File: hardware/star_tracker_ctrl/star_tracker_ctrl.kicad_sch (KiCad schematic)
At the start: 65 parts, among them J1 12V IN, J10 I2C EXP, J11 SPARE IO, J2 CAM USB-A, J20 ESP32 L, J21 ESP32 R, J3 CAM 5V, J30 TMC2209 L, J31 TMC2209 R, J4 MOTOR, J5 DIAG, J6 DS3231, J7 AS5600, J8 HOME, J9 GPS v2, Q1 IRF4905, Q2 IRF4905, Q3 2N3904, SW1 CONFIG, U2 LM2596T-5.0

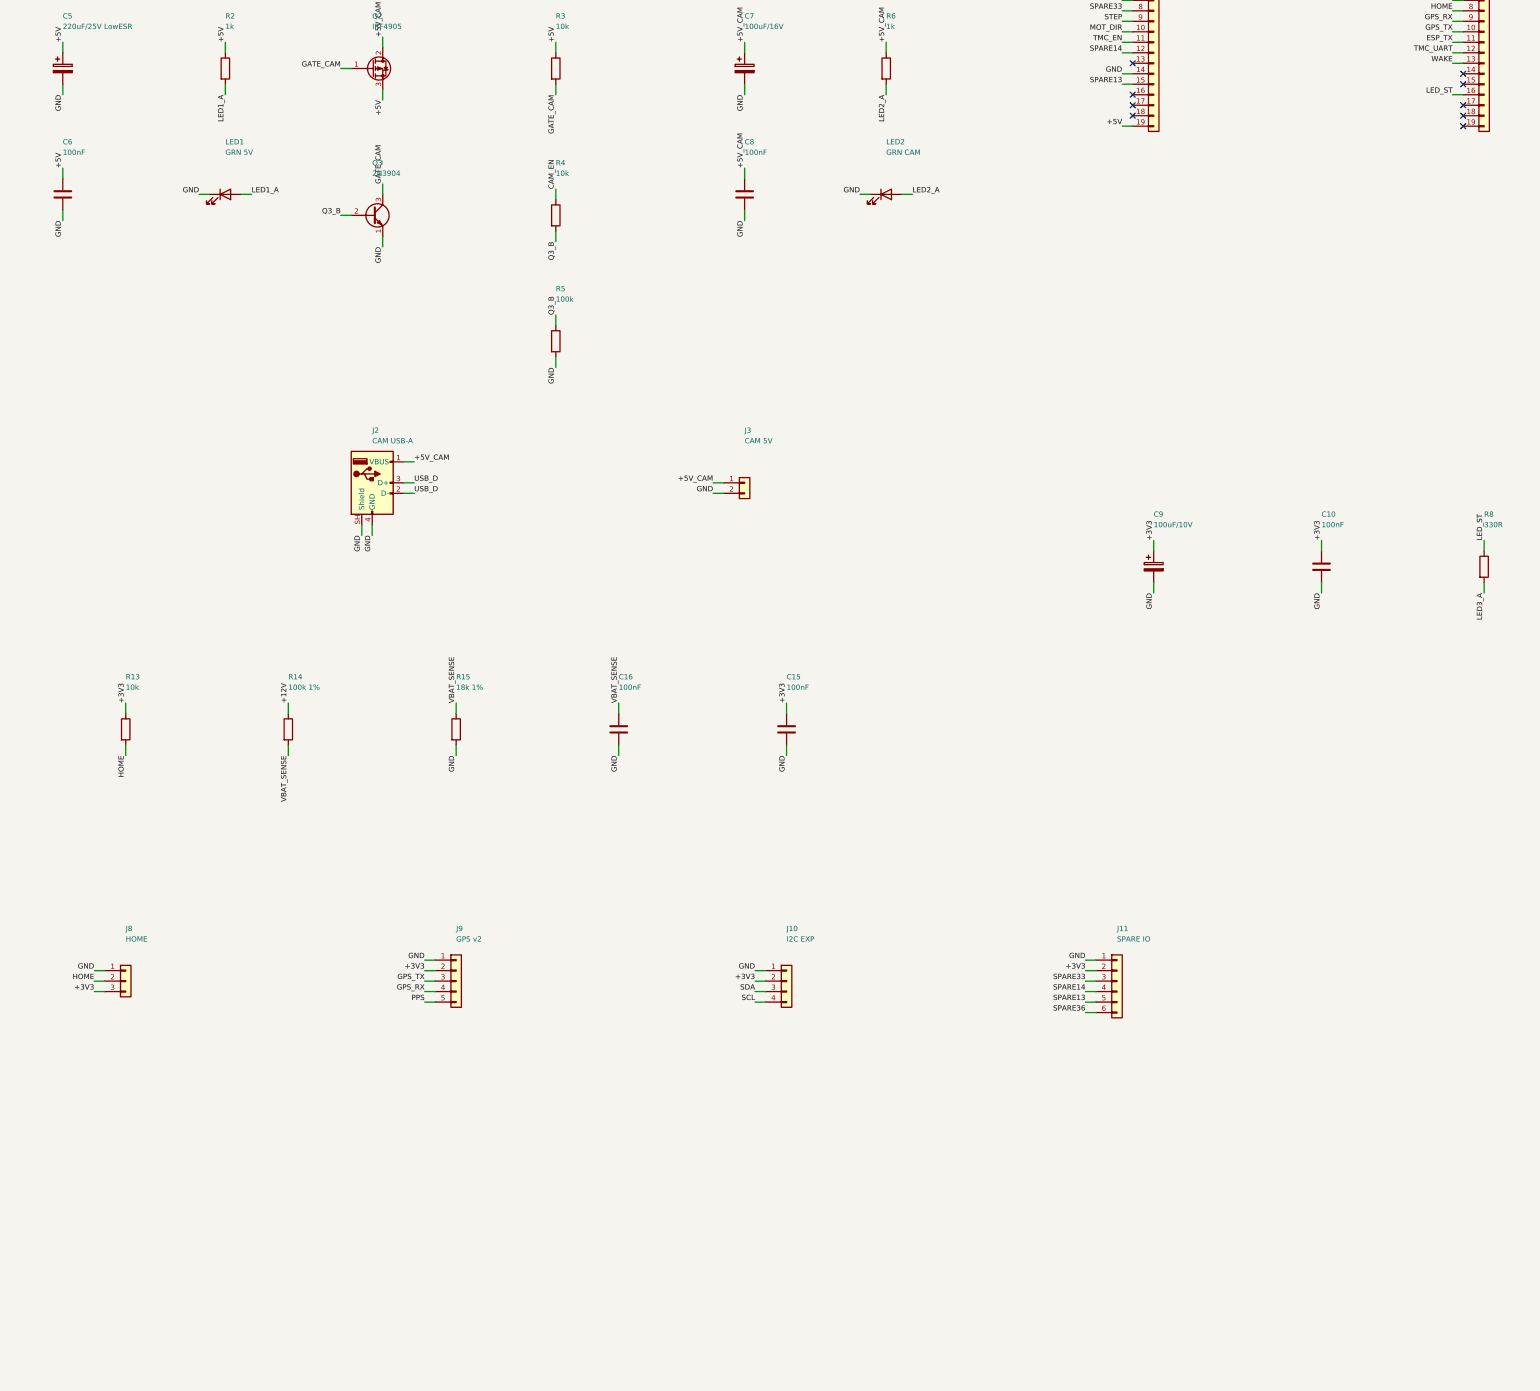
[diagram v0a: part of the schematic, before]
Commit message: Rev B: fix a mirrored ESP32 socket, add GPS, grow the board to 150x100
The important one first. The ESP32 socket in rev A was MIRRORED. The module's
left column was on the top row with pin 1 at the left, and that combination is
neither of the two legal placements -- the transform from module coordinates
to board coordinates had determinant -1, so the module would have had to be
flipped over to fit. Every pin was on the wrong signal. Fabricated, it would
have been scrap with no obvious cause.

A DevKitC laid on its side has exactly two legal orientations:

  90 CW : left column = TOP row, pin 1 at the RIGHT, USB at the LEFT
  90 CCW: left column = BOTTOM row, pin 1 at the LEFT, USB at the RIGHT

Both sockets are now at rotation 270, pin 1 at the right-hand end, USB
pointing left. The rule is written into place.py so it cannot be lost again.

Silkscreen now makes it checkable by eye, which is the real defence: dashed
body outlines for the ESP32 and the TMC2209, a large "USB <<<" at the correct
end, a bold "1" beside pin 1 of all four sockets, per-pin signal names on
every connector, and the orientation stated in words under the module.

GPS is in, as v1 rather than a v2 reservation. A GY-NEO6MV2 supplies time,
date and position; the DS3231 stays, because a GPS cannot wake a sleeping
ESP32 at a time, needs sky view and ~45 mA just to know the time, and has
nothing to say under cloud. The RTC is the bootstrap and the GPS disciplines
it: TIME_SYNC sets the RTC from GPS UTC each evening, records the drift as a
free nightly measurement of the crystal, takes lat/lon for the twilight
calculation, then powers the GPS down. gps_policy defaults to best_effort --
no fix must never cost a night.

The GPS gets a 2N3906 high-side switch off 5 V driven by a 2N3904 on GPIO 2.
Both rails stay up through deep sleep, so an unswitched module would draw
30-45 mA around the clock, roughly 5 Wh a day for a part with ninety seconds
of work each evening. Switched, it costs under 0.1 Wh a nigh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
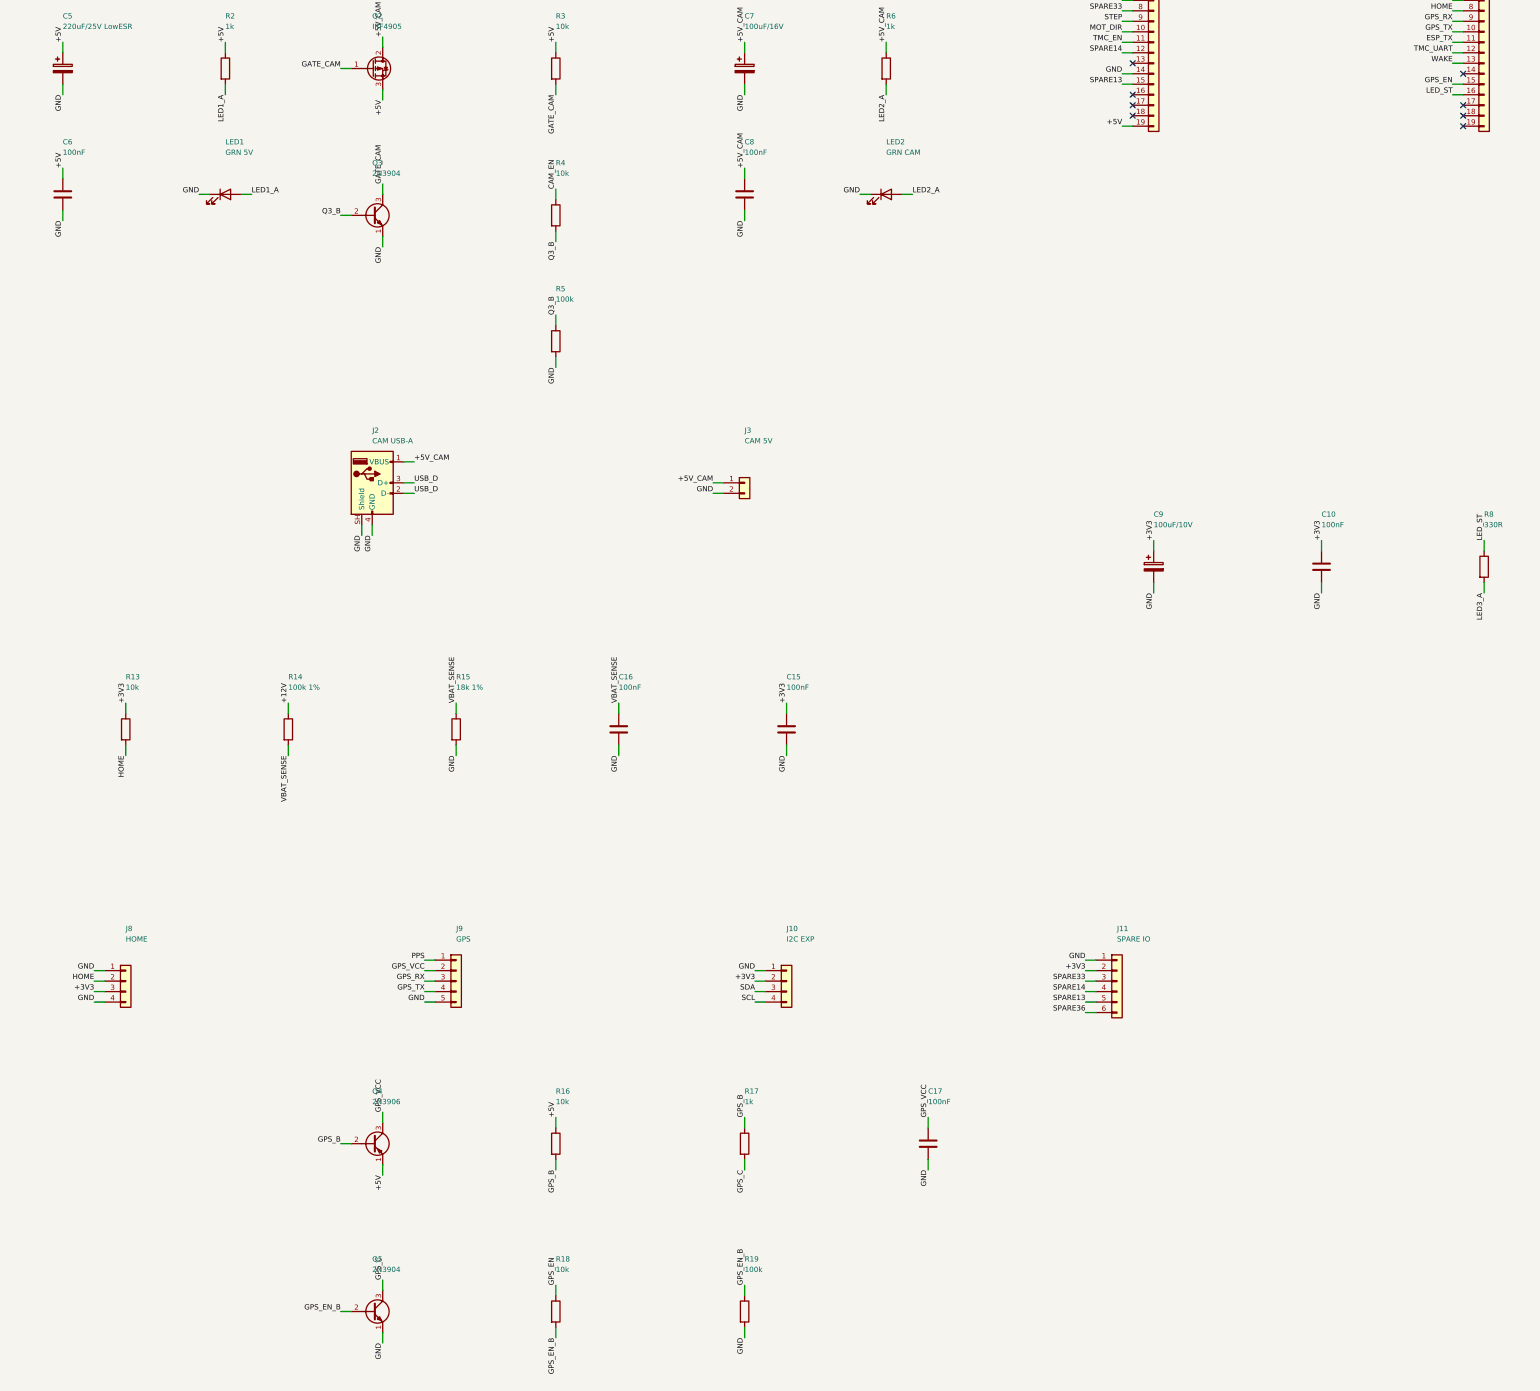
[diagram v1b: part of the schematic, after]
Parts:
- removed J8: HOME, Connector_PinHeader_2.54mm:PinHeader_1x03_P2.54mm_Vertical, symbol Connector_Generic:Conn_01x03
- added C17: 100nF, Capacitor_THT:C_Disc_D5.0mm_W2.5mm_P2.50mm, symbol Device:C
- added J8: HOME, Connector_PinHeader_2.54mm:PinHeader_1x04_P2.54mm_Vertical, symbol Connector_Generic:Conn_01x04
- added Q4: 2N3906, Package_TO_SOT_THT:TO-92_Inline_Wide, symbol Transistor_BJT:2N3906
- added Q5: 2N3904, Package_TO_SOT_THT:TO-92_Inline_Wide, symbol Transistor_BJT:2N3904
- added R16, R18: 10k, Resistor_THT:R_Axial_DIN0207_L6.3mm_D2.5mm_P2.54mm_Vertical, symbol Device:R
- added R17: 1k, Resistor_THT:R_Axial_DIN0207_L6.3mm_D2.5mm_P2.54mm_Vertical, symbol Device:R
- added R19: 100k, Resistor_THT:R_Axial_DIN0207_L6.3mm_D2.5mm_P2.54mm_Vertical, symbol Device:R
- J9: value GPS v2 -> GPS
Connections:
- net +3V3: now also J8.3 (Pin_3); no longer J9.2 (Pin_2)
- net +5V: now also Q4.1 (E), R16.1
- net GND: now also J9.5 (Pin_5), C17.2, J8.1 (Pin_1), J8.4 (Pin_4), Q5.1 (E), R19.2; no longer J9.1 (Pin_1)
- net GPS_RX: now also J9.3 (Pin_3); no longer J9.4 (Pin_4)
- net GPS_TX: now also J9.4 (Pin_4); no longer J9.3 (Pin_3)
- net HOME: now also J8.2 (Pin_2)
- net PPS: now also J9.1 (Pin_1); no longer J9.5 (Pin_5)
- net GPS_EN: now reaches J21.15 (Pin_15)
- net GPS_EN: now also R18.1
- new net GPS_B: Q4.2 (B), R16.2, R17.1
- new net GPS_C: Q5.3 (C), R17.2
- new net GPS_EN_B: Q5.2 (B), R18.2, R19.1
- new net GPS_VCC: C17.1, J9.2 (Pin_2), Q4.3 (C)
- no-connect marks 15 -> 14
